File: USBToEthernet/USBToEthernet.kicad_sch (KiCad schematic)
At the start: 52 parts, among them J1 USB_A, J2 L836-1J1T-43, SW1 SW_Push, U1 LAN7500-ABJZ, U2 NCP1117-3.3_SOT223, U3 93LCxxAxxOT, U4 USBLC6-2SC6, U6 AMS1117-1.2, Y1 25Mhz

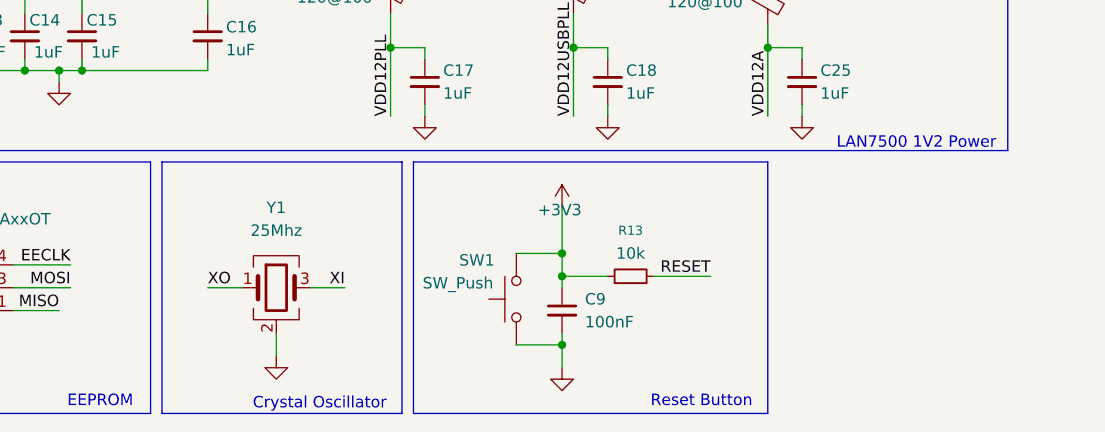
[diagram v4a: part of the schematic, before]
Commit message: Add external load capacitors for oscillator
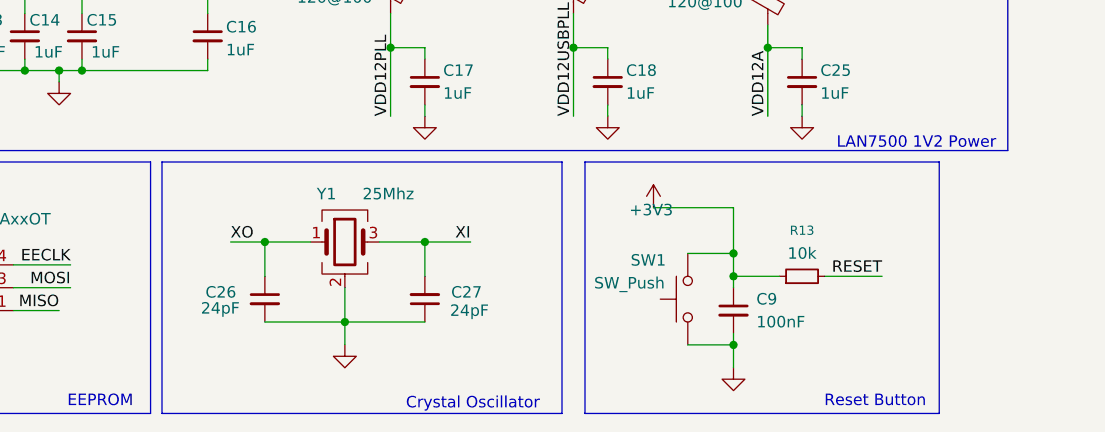
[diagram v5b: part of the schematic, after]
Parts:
- added C26, C27: 24pF, symbol Device:C_Small
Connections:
- net GND: now also C26.2, C27.1
- net XI: now also C27.2
- net XO: now also C26.1
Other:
- moved on the sheet: C9, R13, SW1, Y1

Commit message: Add footprints for the oscillator load capacitors
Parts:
- C26, C27: footprint (none) -> Capacitor_SMD:C_0201_0603Metric
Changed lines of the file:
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@@
 			)
 		)
-		(property "Footprint" ""
+		(property "Footprint" "Capacitor_SMD:C_0201_0603Metric"
 			(at 69.85 184.15 0)
 			(effects
@@
 			)
 		)
-		(property "Footprint" ""
+		(property "Footprint" "Capacitor_SMD:C_0201_0603Metric"
 			(at 87.63 184.15 0)
 			(effects

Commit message: Most placements I think done
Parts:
- C19: footprint Capacitor_SMD:C_0603_1608Metric -> Capacitor_SMD:C_0805_2012Metric
- C26, C27: footprint Capacitor_SMD:C_0201_0603Metric -> Capacitor_SMD:C_0603_1608Metric
- R10, R11, R12, R5, R6, R7, R8, R9: footprint Resistor_SMD:R_0201_0603Metric -> Resistor_SMD:R_0603_1608Metric
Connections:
- net +3V3: no longer C9.1, SW1.2
- net RESET: now also C9.1, SW1.2
- net D+Out renamed DOut+
- net D-Out renamed DOut-
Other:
- moved on the sheet: R13
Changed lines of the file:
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@@
 	(wire
 		(pts
-			(xy 132.08 181.61) (xy 138.43 181.61)
-		)
-		(stroke
-			(width 0)
-			(type default)
-		)
-	)
-	(wire
-		(pts
 			(xy 175.26 25.4) (xy 175.26 29.21)
 		)
@@
 	(wire
 		(pts
-			(xy 121.92 181.61) (xy 127 181.61)
+			(xy 121.92 181.61) (xy 138.43 181.61)
 		)
 		(stroke
@@
 	(wire
 		(pts
+			(xy 121.92 172.72) (xy 121.92 171.45)
+		)
+		(stroke
+			(width 0)
+			(type default)
+		)
+	)
+	(wire
+		(pts
 			(xy 41.91 180.34) (xy 48.26 180.34)
 		)
@@
 	(wire
 		(pts
+			(xy 158.75 60.96) (xy 158.75 62.23)
+		)
+		(stroke
+			(width 0)
+			(type default)
+		)
+	)
+	(wire
+		(pts
 			(xy 149.86 73.66) (xy 149.86 78.74)
 		)
@@
 	(wire
 		(pts
-			(xy 121.92 173.99) (xy 121.92 179.07)
-		)
-		(stroke
-			(width 0)
-			(type default)
-		)
-	)
-	(wire
-		(pts
 			(xy 234.95 88.9) (xy 246.38 88.9)
 		)
@@
 	(wire
 		(pts
+			(xy 121.92 177.8) (xy 121.92 179.07)
+		)
+		(stroke
+			(width 0)
+			(type default)
+		)
+	)
+	(wire
+		(pts
 			(xy 31.75 173.99) (xy 31.75 175.26)
 		)
@@
 	(wire
 		(pts
-			(xy 121.92 173.99) (xy 113.03 173.99)
-		)
-		(stroke
-			(width 0)
-			(type default)
-		)
-	)
-	(wire
-		(pts
 			(xy 175.26 29.21) (xy 175.26 39.37)
 		)
@@
 		)
 	)
-	(label "D+Out"
+	(label "DOut+"
 		(at 91.44 85.09 0)
 		(effects
@@
 		)
 	)
-	(label "D-Out"
+	(label "DOut-"
 		(at 91.44 87.63 0)
 		(effects
@@
 		)
 	)
-	(label "D+Out"
+	(label "DOut+"
 		(at 74.93 39.37 180)
 		(effects
@@
 		)
 	)
-	(label "D-Out"
+	(label "DOut-"
 		(at 74.93 36.83 180)
 		(effects
@@
 			)
 		)
-		(property "Footprint" "Resistor_SMD:R_0201_0603Metric"
+		(property "Footprint" "Resistor_SMD:R_0603_1608Metric"
 			(at 196.85 30.48 0)
 			(effects
@@
 			)
 		)
-		(property "Footprint" "Capacitor_SMD:C_0201_0603Metric"
+		(property "Footprint" "Capacitor_SMD:C_0603_1608Metric"
 			(at 69.85 184.15 0)
 			(effects
@@
 	(symbol
 		(lib_id "power:+3V3")
-		(at 113.03 173.99 0)
+		(at 121.92 171.45 0)
 		(unit 1)
 		(exclude_from_sim no)
@@
 		(dnp no)
 		(property "Reference" "#PWR023"
-			(at 113.03 177.8 0)
+			(at 121.92 175.26 0)
 			(effects
 				(font
@@
 		)
 		(property "Value" "+3V3"
-			(at 112.776 174.244 0)
+			(at 117.348 170.434 0)
 			(effects
 				(font
@@
 		)
 		(property "Footprint" ""
-			(at 113.03 173.99 0)
+			(at 121.92 171.45 0)
 			(effects
 				(font
@@
 		)
 		(property "Datasheet" ""
-			(at 113.03 173.99 0)
+			(at 121.92 171.45 0)
 			(effects
 				(font
@@
 		)
 		(property "Description" "Power symbol creates a global label with name \"+3V3\""
-			(at 113.03 173.99 0)
+			(at 121.92 171.45 0)
 			(effects
 				(font
@@
 			)
 		)
-		(property "Footprint" "Resistor_SMD:R_0201_0603Metric"
+		(property "Footprint" "Resistor_SMD:R_0603_1608Metric"
 			(at 264.16 30.48 0)
 			(effects
@@
 			)
 		)
-		(property "Footprint" "Resistor_SMD:R_0201_0603Metric"
+		(property "Footprint" "Resistor_SMD:R_0603_1608Metric"
 			(at 200.66 30.48 0)
 			(effects
@@
 			)
 		)
-		(property "Footprint" "Capacitor_SMD:C_0603_1608Metric"
+		(property "Footprint" "Capacitor_SMD:C_0805_2012Metric"
 			(at 66.04 24.13 0)
 			(effects
@@
 			)
 		)
-		(property "Footprint" "Resistor_SMD:R_0201_0603Metric"
+		(property "Footprint" "Resistor_SMD:R_0603_1608Metric"
 			(at 260.35 30.48 0)
 			(effects
@@
 			)
 		)
-		(property "Footprint" "Resistor_SMD:R_0201_0603Metric"
+		(property "Footprint" "Resistor_SMD:R_0603_1608Metric"
 			(at 163.83 30.48 0)
 			(effects
@@
 	(symbol
 		(lib_id "power:+3V3")
-		(at 158.75 62.23 0)
+		(at 158.75 60.96 0)
 		(unit 1)
 		(exclude_from_sim no)
@@
 		(fields_autoplaced yes)
 		(property "Reference" "#PWR028"
-			(at 158.75 66.04 0)
+			(at 158.75 64.77 0)
 			(effects
 				(font
@@
 		)
 		(property "Value" "+3V3"
-			(at 158.75 57.15 0)
+			(at 158.75 55.88 0)
 			(effects
 				(font
@@
 		)
 		(property "Footprint" ""
-			(at 158.75 62.23 0)
+			(at 158.75 60.96 0)
 			(effects
 				(font
@@
 		)
 		(property "Datasheet" ""
-			(at 158.75 62.23 0)
+			(at 158.75 60.96 0)
 			(effects
 				(font
@@
 		)
 		(property "Description" "Power symbol creates a global label with name \"+3V3\""
-			(at 158.75 62.23 0)
+			(at 158.75 60.96 0)
 			(effects
 				(font
@@
 			)
 		)
-		(property "Footprint" "Capacitor_SMD:C_0201_0603Metric"
+		(property "Footprint" "Capacitor_SMD:C_0603_1608Metric"
 			(at 87.63 184.15 0)
 			(effects
@@
 			)
 		)
-		(property "Footprint" "Resistor_SMD:R_0201_0603Metric"
+		(property "Footprint" "Resistor_SMD:R_0603_1608Metric"
 			(at 228.6 30.48 0)
 			(effects
@@
 			)
 		)
-		(property "Footprint" "Resistor_SMD:R_0201_0603Metric"
+		(property "Footprint" "Resistor_SMD:R_0603_1608Metric"
 			(at 167.64 30.48 0)
 			(effects
@@
 	(symbol
 		(lib_id "Device:R_Small")
-		(at 129.54 181.61 90)
+		(at 121.92 175.26 0)
 		(unit 1)
 		(exclude_from_sim no)
@@
 		(fields_autoplaced yes)
 		(property "Reference" "R13"
-			(at 129.54 176.53 90)
+			(at 124.46 173.9899 0)
 			(effects
 				(font
 					(size 1.016 1.016)
 				)
+				(justify left)
 			)
 		)
 		(property "Value" "10k"
-			(at 129.54 179.07 90)
+			(at 124.46 176.5299 0)
 			(effects
 				(font
 					(size 1.27 1.27)
 				)
+				(justify left)
 			)
 		)
 		(property "Footprint" "Resistor_SMD:R_0603_1608Metric"
-			(at 129.54 181.61 0)
+			(at 121.92 175.26 0)
 			(effects
 				(font
@@
 		)
 		(property "Datasheet" "~"
-			(at 129.54 181.61 0)
+			(at 121.92 175.26 0)
 			(effects
 				(font
@@
 		)
 		(property "Description" "Resistor, small symbol"
-			(at 129.54 181.61 0)
+			(at 121.92 175.26 0)
 			(effects
 				(font
@@
 			)
 		)
-		(property "Footprint" "Resistor_SMD:R_0201_0603Metric"
+		(property "Footprint" "Resistor_SMD:R_0603_1608Metric"
 			(at 232.41 30.48 0)
 			(effects

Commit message: Fried ahh PCB layout and routing
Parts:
- removed J1: USB_A, USB_AP_S_RA_SMT:CONN_USB-AP-S-RA-SMT_ADM, symbol Connector:USB_A
- added J1: 0480372200, symbol USB_A_Plug:0480372200
- C19: footprint Capacitor_SMD:C_0805_2012Metric -> Capacitor_SMD:C_0603_1608Metric
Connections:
- net D+: now also J1.2 (D-)
- net D-: now also J1.3 (D+)
- net GND: now also J1.4 (GND), J1.S1 (SHIELD)
- net VBUS: now also J1.1 (VBUS)
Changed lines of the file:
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@@
 	)
 	(junction
-		(at 29.21 26.67)
-		(diameter 0)
-		(color 0 0 0 0)
-	)
-	(junction
 		(at 46.99 158.75)
 		(diameter 0)
@@
 	(wire
 		(pts
-			(xy 25.4 26.67) (xy 29.21 26.67)
+			(xy 29.21 27.94) (xy 39.37 27.94)
 		)
 		(stroke
@@
 		)
 	)
-	(wire
-		(pts
-			(xy 29.21 26.67) (xy 41.91 26.67)
-		)
-		(stroke
-			(width 0)
-			(type default)
-		)
-	)
 	(polyline
 		(pts
@@
 	)
 	(label "VBUS"
-		(at 40.64 26.67 180)
+		(at 38.1 27.94 180)
 		(effects
 			(font
@@
 	)
 	(symbol
-		(lib_id "Connector:USB_A")
-		(at 21.59 31.75 0)
-		(unit 1)
-		(exclude_from_sim no)
-		(in_bom yes)
-		(on_board yes)
-		(dnp no)
-		(fields_autoplaced yes)
-		(property "Reference" "J1"
-			(at 21.59 19.05 0)
-			(effects
-				(font
-					(size 1.27 1.27)
-				)
-			)
-		)
-		(property "Value" "USB_A"
-			(at 21.59 21.59 0)
-			(effects
-				(font
-					(size 1.27 1.27)
-				)
-			)
-		)
-		(property "Footprint" "USB_AP_S_RA_SMT:CONN_USB-AP-S-RA-SMT_ADM"
-			(at 25.4 33.02 0)
-			(effects
-				(font
-					(size 1.27 1.27)
-				)
-				(hide yes)
-			)
-		)
-		(property "Datasheet" "~"
-			(at 25.4 33.02 0)
-			(effects
-				(font
-					(size 1.27 1.27)
-				)
-				(hide yes)
-			)
-		)
-		(property "Description" "USB Type A connector"
-			(at 21.59 31.75 0)
-			(effects
-				(font
-					(size 1.27 1.27)
-				)
-				(hide yes)
-			)
-		)
-		(pin "2"
-		)
-		(pin "3"
-		)
-		(pin "4"
-		)
-		(pin "1"
-		)
-		(pin "5"
-		)
-		(instances
-			(project ""
-				(path "/e2f4c3a6-d848-4365-9cff-800700e3d63d"
-					(reference "J1")
-					(unit 1)
-				)
-			)
-		)
-	)
-	(symbol
 		(lib_id "Device:C_Small")
 		(at 129.54 160.02 0)
@@
 	(symbol
 		(lib_id "power:PWR_FLAG")
-		(at 41.91 26.67 0)
+		(at 39.37 27.94 0)
 		(unit 1)
 		(exclude_from_sim no)
@@
 		(dnp no)
 		(property "Reference" "#FLG08"
-			(at 41.91 24.765 0)
+			(at 39.37 26.035 0)
 			(effects
 				(font
@@
 		)
 		(property "Value" "PWR_FLAG"
-			(at 48.006 25.146 0)
+			(at 45.466 26.416 0)
 			(effects
 				(font
@@
 		)
 		(property "Footprint" ""
-			(at 41.91 26.67 0)
+			(at 39.37 27.94 0)
 			(effects
 				(font
@@
 		)
 		(property "Datasheet" "~"
-			(at 41.91 26.67 0)
+			(at 39.37 27.94 0)
 			(effects
 				(font
@@
 		)
 		(property "Description" "Special symbol for telling ERC where power comes from"
-			(at 41.91 26.67 0)
+			(at 39.37 27.94 0)
 			(effects
 				(font
@@
 			)
 		)
-		(property "Footprint" "Capacitor_SMD:C_0805_2012Metric"
+		(property "Footprint" "Capacitor_SMD:C_0603_1608Metric"
 			(at 66.04 24.13 0)
 			(effects
@@
 					(unit 1)
 				)
+			)
+		)
+	)
+	(symbol
+		(lib_id "USB_A_Plug:0480372200")
+		(at 21.59 33.02 0)
+		(unit 1)
+		(exclude_from_sim no)
+		(in_bom yes)
+		(on_board yes)
+		(dnp no)
+		(fields_autoplaced yes)
+		(property "Reference" "J1"
+			(at 21.59 20.32 0)
+			(effects
+				(font
+					(size 1.27 1.27)
+				)
+			)
+		)
+		(property "Value" "0480372200"
+			(at 21.59 22.86 0)
+			(effects
+				(font
+					(size 1.27 1.27)
+				)
+			)
+		)
+		(property "Footprint" ""
+			(at 19.812 16.256 0)
+			(effects
+				(font
+					(size 1.27 1.27)
+				)
+				(justify bottom)
+				(hide yes)
+			)
+		)
+		(property "Datasheet" ""
+			(at 21.59 33.02 0)
+			(effects
+				(font
+					(size 1.27 1.27)
+				)
+				(hide yes)
+			)
+		)
+		(property "Description" ""
+			(at 21.59 33.02 0)
+			(effects
+				(font
+					(size 1.27 1.27)
+				)
+				(hide yes)
+			)
+		)
+		(property "DigiKey_Part_Number" ""
+			(at 35.306 27.178 0)
+			(effects
+				(font
+					(size 1.27 1.27)
+				)
+				(justify bottom)
+				(hide yes)
+			)
+		)
+		(property "SnapEDA_Link" ""
+			(at 21.59 33.02 0)
+			(effects
+				(font
+					(size 1.27 1.27)
+				)
+				(justify bottom)
+				(hide yes)
+			)
+		)
+		(property "MAXIMUM_PACKAGE_HEIGHT" ""
+			(at 36.068 33.02 0)
+			(effects
+				(font
+					(size 1.27 1.27)
+				)
+				(justify bottom)
+				(hide yes)
+			)
+		)
+		(property "Package" ""
+			(at 37.338 40.386 0)
+			(effects
+				(font
+					(size 1.27 1.27)
+				)
+				(justify bottom)
+				(hide yes)
+			)
+		)
+		(property "Check_prices" ""
+			(at 20.32 23.114 0)
+			(effects
+				(font
+					(size 1.27 1.27)
+				)
+				(justify bottom)
+				(hide yes)
+			)
+		)
+		(property "STANDARD" ""
+			(at 21.336 20.574 0)
+			(effects
+				(font
+					(size 1.27 1.27)
+				)
+				(justify bottom)
+				(hide yes)
+			)
+		)
+		(property "PARTREV" ""
+			(at 35.052 39.624 0)
+			(effects
+				(font
+					(size 1.27 1.27)
+				)
+				(justify bottom)
+				(hide yes)
+			)
+		)
+		(property "MF" ""
+			(at 21.59 33.02 0)
+			(effects
+				(font
+					(size 1.27 1.27)
+				)
+				(justify bottom)
+				(hide yes)
+			)
+		)
+		(property "MP" ""
+			(at 21.082 25.146 0)
+			(effects
+				(font
+					(size 1.27 1.27)
+				)
+				(justify bottom)
+				(hide yes)
+			)
+		)
+		(property "Description_1" ""
+			(at 21.59 33.02 0)
+			(effects
+				(font
+					(size 1.27 1.27)
+				)
+				(justify bottom)
+				(hide yes)
+			)
+		)
+		(property "MANUFACTURER" ""
+			(at 21.59 33.02 0)
+			(effects
+				(font
+					(size 1.27 1.27)
+				)
+				(justify bottom)
+				(hide yes)
+			)
+		)
+		(pin "S1"
+		)
+		(pin "4"
+		)
+		(pin "1"
+		)
+		(pin "2"
+		)
+		(pin "3"
+		)
+		(instances
+			(project ""
+				(path "/e2f4c3a6-d848-4365-9cff-800700e3d63d"
+					(reference "J1")
+					(unit 1)
+				)
